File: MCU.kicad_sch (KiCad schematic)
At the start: 26 parts, among them J1 FTSH-105-01-L-DV-K-A, J2 USB_C_Receptacle_USB2.0_16P, U1 STM32G0B1CBTx, Y1 Crystal_GND24, Y2 32.768 kHz 6pF

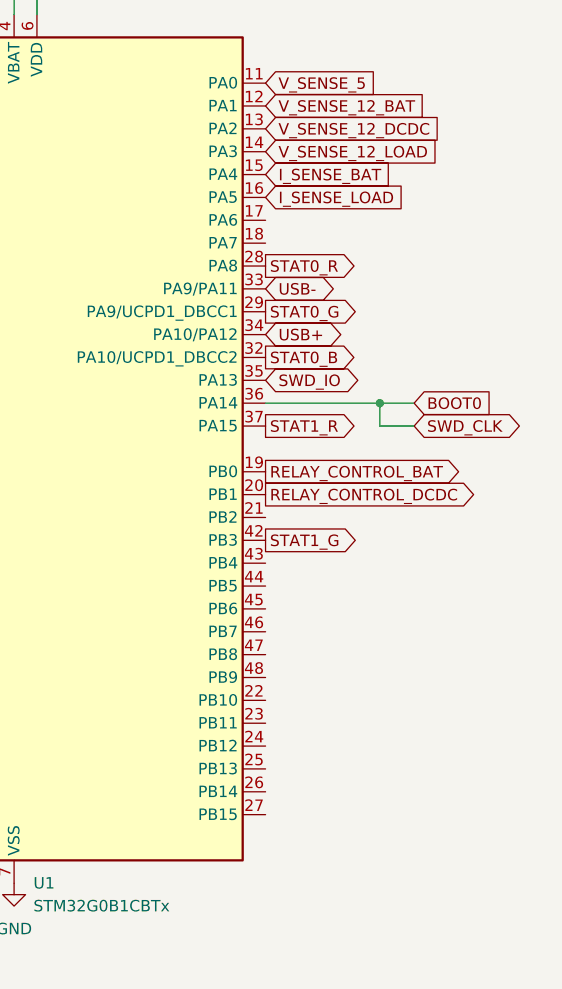
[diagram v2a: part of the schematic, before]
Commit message: schematic changes and initial routing
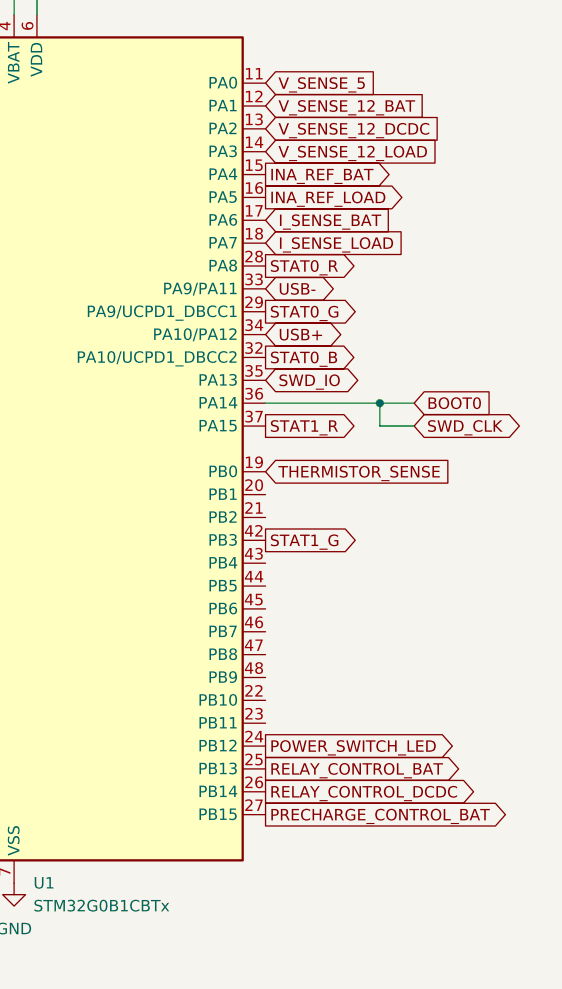
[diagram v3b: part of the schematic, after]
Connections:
- net I_SENSE_BAT: now also U1.17 (PA6); no longer U1.15 (PA4)
- net I_SENSE_LOAD: now also U1.18 (PA7); no longer U1.16 (PA5)
- net RELAY_CONTROL_BAT: now also U1.25 (PB13); no longer U1.19 (PB0)
- net RELAY_CONTROL_DCDC: now also U1.26 (PB14); no longer U1.20 (PB1)
- net POWER_SWITCH_LED: now reaches U1.24 (PB12)
- net PRECHARGE_CONTROL_BAT: now reaches U1.27 (PB15)
- new net INA_REF_BAT: U1.15 (PA4)
- new net INA_REF_LOAD: U1.16 (PA5)
- new net THERMISTOR_SENSE: U1.19 (PB0)
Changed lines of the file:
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@@
 	(global_label "I_SENSE_LOAD"
 		(shape input)
-		(at 248.92 53.34 0)
-		(fields_autoplaced yes)
-		(effects
-			(font
-				(size 1.27 1.27)
-			)
-			(justify left)
-		)
-		(property "Intersheetrefs" "${INTERSHEET_REFS}"
-			(at 265.2099 53.34 0)
+		(at 248.92 58.42 0)
+		(fields_autoplaced yes)
+		(effects
+			(font
+				(size 1.27 1.27)
+			)
+			(justify left)
+		)
+		(property "Intersheetrefs" "${INTERSHEET_REFS}"
+			(at 265.2099 58.42 0)
 			(hide yes)
 			(show_name no)
@@
 		)
 	)
+	(global_label "PRECHARGE_CONTROL_BAT"
+		(shape output)
+		(at 248.92 121.92 0)
+		(fields_autoplaced yes)
+		(effects
+			(font
+				(size 1.27 1.27)
+			)
+			(justify left)
+		)
+		(property "Intersheetrefs" "${INTERSHEET_REFS}"
+			(at 276.7609 121.92 0)
+			(hide yes)
+			(show_name no)
+			(do_not_autoplace no)
+			(effects
+				(font
+					(size 1.27 1.27)
+				)
+				(justify left)
+			)
+		)
+	)
 	(global_label "BTN_USR1"
 		(shape output)
@@
 	(global_label "RELAY_CONTROL_BAT"
 		(shape output)
-		(at 248.92 83.82 0)
-		(fields_autoplaced yes)
-		(effects
-			(font
-				(size 1.27 1.27)
-			)
-			(justify left)
-		)
-		(property "Intersheetrefs" "${INTERSHEET_REFS}"
-			(at 271.3181 83.82 0)
+		(at 248.92 116.84 0)
+		(fields_autoplaced yes)
+		(effects
+			(font
+				(size 1.27 1.27)
+			)
+			(justify left)
+		)
+		(property "Intersheetrefs" "${INTERSHEET_REFS}"
+			(at 271.3181 116.84 0)
 			(hide yes)
 			(show_name no)
@@
 		(property "Intersheetrefs" "${INTERSHEET_REFS}"
 			(at 267.6893 43.18 0)
+			(hide yes)
+			(show_name no)
+			(do_not_autoplace no)
+			(effects
+				(font
+					(size 1.27 1.27)
+				)
+				(justify left)
+			)
+		)
+	)
+	(global_label "INA_REF_LOAD"
+		(shape output)
+		(at 248.92 53.34 0)
+		(fields_autoplaced yes)
+		(effects
+			(font
+				(size 1.27 1.27)
+			)
+			(justify left)
+		)
+		(property "Intersheetrefs" "${INTERSHEET_REFS}"
+			(at 265.0891 53.34 0)
 			(hide yes)
 			(show_name no)
@@
 		)
 	)
+	(global_label "POWER_SWITCH_LED"
+		(shape output)
+		(at 248.92 114.3 0)
+		(fields_autoplaced yes)
+		(effects
+			(font
+				(size 1.27 1.27)
+			)
+			(justify left)
+		)
+		(property "Intersheetrefs" "${INTERSHEET_REFS}"
+			(at 270.5922 114.3 0)
+			(hide yes)
+			(show_name no)
+			(do_not_autoplace no)
+			(effects
+				(font
+					(size 1.27 1.27)
+				)
+				(justify left)
+			)
+		)
+	)
 	(global_label "HSE_OUT"
 		(shape input)
@@
 				)
 				(justify right)
+			)
+		)
+	)
+	(global_label "THERMISTOR_SENSE"
+		(shape input)
+		(at 248.92 83.82 0)
+		(fields_autoplaced yes)
+		(effects
+			(font
+				(size 1.27 1.27)
+			)
+			(justify left)
+		)
+		(property "Intersheetrefs" "${INTERSHEET_REFS}"
+			(at 270.4712 83.82 0)
+			(hide yes)
+			(show_name no)
+			(do_not_autoplace no)
+			(effects
+				(font
+					(size 1.27 1.27)
+				)
+				(justify left)
 			)
 		)
@@
 		)
 	)
-	(global_label "RELAY_CONTROL_DCDC"
-		(shape output)
-		(at 248.92 86.36 0)
-		(fields_autoplaced yes)
-		(effects
-			(font
-				(size 1.27 1.27)
-			)
-			(justify left)
-		)
-		(property "Intersheetrefs" "${INTERSHEET_REFS}"
-			(at 273.0719 86.36 0)
-			(hide yes)
-			(show_name no)
-			(do_not_autoplace no)
-			(effects
-				(font
-					(size 1.27 1.27)
-				)
-				(justify left)
-			)
-		)
-	)
 	(global_label "V_SENSE_12_LOAD"
 		(shape input)
@@
 	(global_label "I_SENSE_BAT"
 		(shape input)
-		(at 248.92 50.8 0)
-		(fields_autoplaced yes)
-		(effects
-			(font
-				(size 1.27 1.27)
-			)
-			(justify left)
-		)
-		(property "Intersheetrefs" "${INTERSHEET_REFS}"
-			(at 263.8189 50.8 0)
+		(at 248.92 55.88 0)
+		(fields_autoplaced yes)
+		(effects
+			(font
+				(size 1.27 1.27)
+			)
+			(justify left)
+		)
+		(property "Intersheetrefs" "${INTERSHEET_REFS}"
+			(at 263.8189 55.88 0)
 			(hide yes)
 			(show_name no)
@@
 		)
 	)
+	(global_label "RELAY_CONTROL_DCDC"
+		(shape output)
+		(at 248.92 119.38 0)
+		(fields_autoplaced yes)
+		(effects
+			(font
+				(size 1.27 1.27)
+			)
+			(justify left)
+		)
+		(property "Intersheetrefs" "${INTERSHEET_REFS}"
+			(at 273.0719 119.38 0)
+			(hide yes)
+			(show_name no)
+			(do_not_autoplace no)
+			(effects
+				(font
+					(size 1.27 1.27)
+				)
+				(justify left)
+			)
+		)
+	)
 	(global_label "STAT1_G"
 		(shape input)
@@
 			(hide yes)
 			(show_name no)
+			(do_not_autoplace no)
+			(effects
+				(font
+					(size 1.27 1.27)
+				)
+				(justify left)
+			)
+		)
+	)
+	(global_label "INA_REF_BAT"
+		(shape output)
+		(at 248.92 50.8 0)
+		(fields_autoplaced yes)
+		(effects
+			(font
+				(size 1.27 1.27)
+			)
+			(justify left)
+		)
+		(property "Intersheetrefs" "${INTERSHEET_REFS}"
+			(at 263.6981 50.8 0)
+			(hide yes)
+			(show_name no)

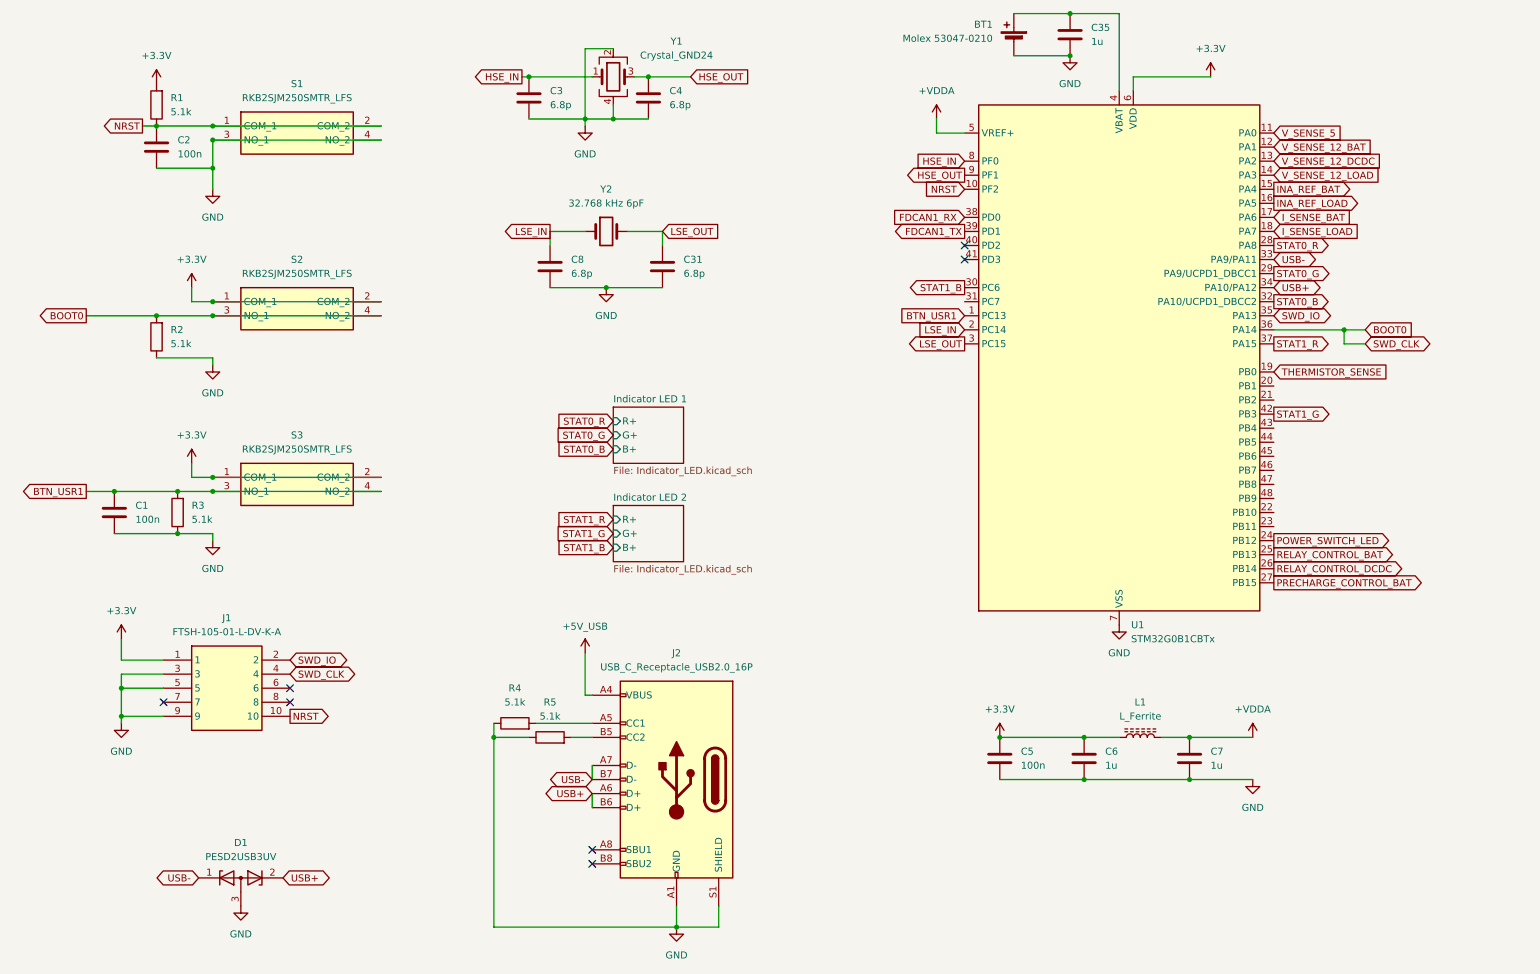
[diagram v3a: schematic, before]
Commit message: finished layout, routing, and silkscreen
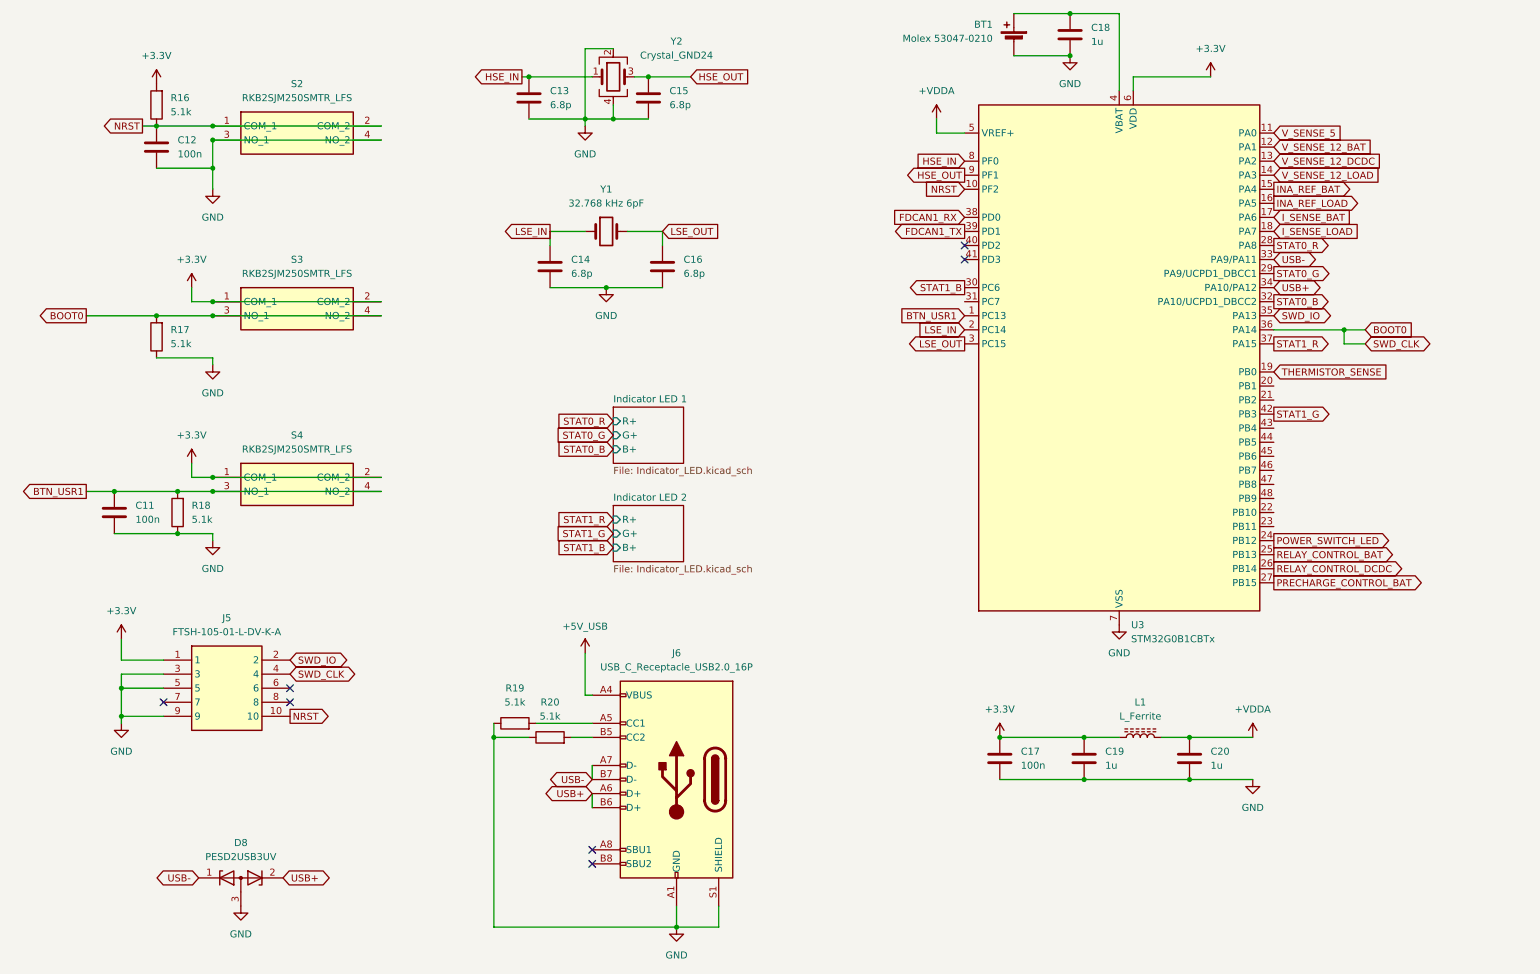
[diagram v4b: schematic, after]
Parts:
- renumbered C1 to C11, C2 to C12, C3 to C13, C8 to C14, C4 to C15, C31 to C16, C5 to C17, C35 to C18, C6 to C19, C7 to C20, D1 to D8, J1 to J5, J2 to J6, R1 to R16, R2 to R17, R3 to R18, R4 to R19, R5 to R20, S1 to S2, S2 to S3, S3 to S4, U1 to U3, Y2 to Y1, Y1 to Y2

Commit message: minor layout and silkscreen tweaks
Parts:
- added J9: Conn_01x09, Connector_PinHeader_2.54mm:PinHeader_1x09_P2.54mm_Vertical, symbol Connector_Generic:Conn_01x09
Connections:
- net +3.3V: now also J9.3 (Pin_3)
- net GND: now also J9.1 (Pin_1)
- net at U3.43 (PB4): now also J9.4 (Pin_4)
- net at U3.44 (PB5): now also J9.5 (Pin_5)
- net at U3.45 (PB6): now also J9.6 (Pin_6)
- net at U3.46 (PB7): now also J9.7 (Pin_7)
- net at U3.47 (PB8): now also J9.8 (Pin_8)
- net at U3.48 (PB9): now also J9.9 (Pin_9)
- new net +5V: J9.2 (Pin_2)

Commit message: r0 final
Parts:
- renumbered D8 to D5, J9 to J7
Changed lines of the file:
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@@
 		(dnp no)
 		(fields_autoplaced yes)
-		(property "Reference" "D8"
+		(property "Reference" "D5"
 			(at 62.23 168.91 0)
 			(show_name no)
@@
 			(project "RSC-LV3-LVBPS"
 				(path "/4bbf2fff-9f66-421d-84bf-68d1dcd1e11d/4b8add19-2d3e-4ee3-9fc6-a72eb5b6d291"
-					(reference "D8")
+					(reference "D5")
 					(unit 1)
 				)
@@
 		(dnp no)
 		(fields_autoplaced yes)
-		(property "Reference" "#PWR071"
+		(property "Reference" "#PWR045"
 			(at 278.13 90.17 0)
 			(hide yes)
@@
 			(project "RSC-LV3-LVBPS"
 				(path "/4bbf2fff-9f66-421d-84bf-68d1dcd1e11d/4b8add19-2d3e-4ee3-9fc6-a72eb5b6d291"
-					(reference "#PWR071")
+					(reference "#PWR045")
 					(unit 1)
 				)
@@
 		(dnp no)
 		(fields_autoplaced yes)
-		(property "Reference" "J9"
+		(property "Reference" "J7"
 			(at 281.94 96.5199 0)
 			(show_name no)
@@
 			(project "RSC-LV3-LVBPS"
 				(path "/4bbf2fff-9f66-421d-84bf-68d1dcd1e11d/4b8add19-2d3e-4ee3-9fc6-a72eb5b6d291"
-					(reference "J9")
+					(reference "J7")
 					(unit 1)
 				)
@@
 		(dnp no)
 		(fields_autoplaced yes)
-		(property "Reference" "#PWR072"
+		(property "Reference" "#PWR046"
 			(at 278.13 92.71 0)
 			(hide yes)
@@
 			(project "RSC-LV3-LVBPS"
 				(path "/4bbf2fff-9f66-421d-84bf-68d1dcd1e11d/4b8add19-2d3e-4ee3-9fc6-a72eb5b6d291"
-					(reference "#PWR072")
+					(reference "#PWR046")
 					(unit 1)
 				)
@@
 		(dnp no)
 		(fields_autoplaced yes)
-		(property "Reference" "#PWR070"
+		(property "Reference" "#PWR044"
 			(at 267.97 87.63 0)
 			(hide yes)
@@
 			(project "RSC-LV3-LVBPS"
 				(path "/4bbf2fff-9f66-421d-84bf-68d1dcd1e11d/4b8add19-2d3e-4ee3-9fc6-a72eb5b6d291"
-					(reference "#PWR070")
+					(reference "#PWR044")
 					(unit 1)
 				)
